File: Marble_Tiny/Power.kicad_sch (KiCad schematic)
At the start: 63 parts, among them J10 Barrel_Jack_Switch, Q4 DMP3013SFV, U10 TPSM863257RDXR, U11 TPSM863257RDXR, U18 TLV77325PDBVR, U20 RT9045AGSP / AP2303, U23 NCV59801CML120TCG, U24 SN74LVC1G07DBV, U25 SN74LVC1G07DBV, U4 TPSM863257RDXR, U5 TPSM863257RDXR, U6 TPSM863257RDXR

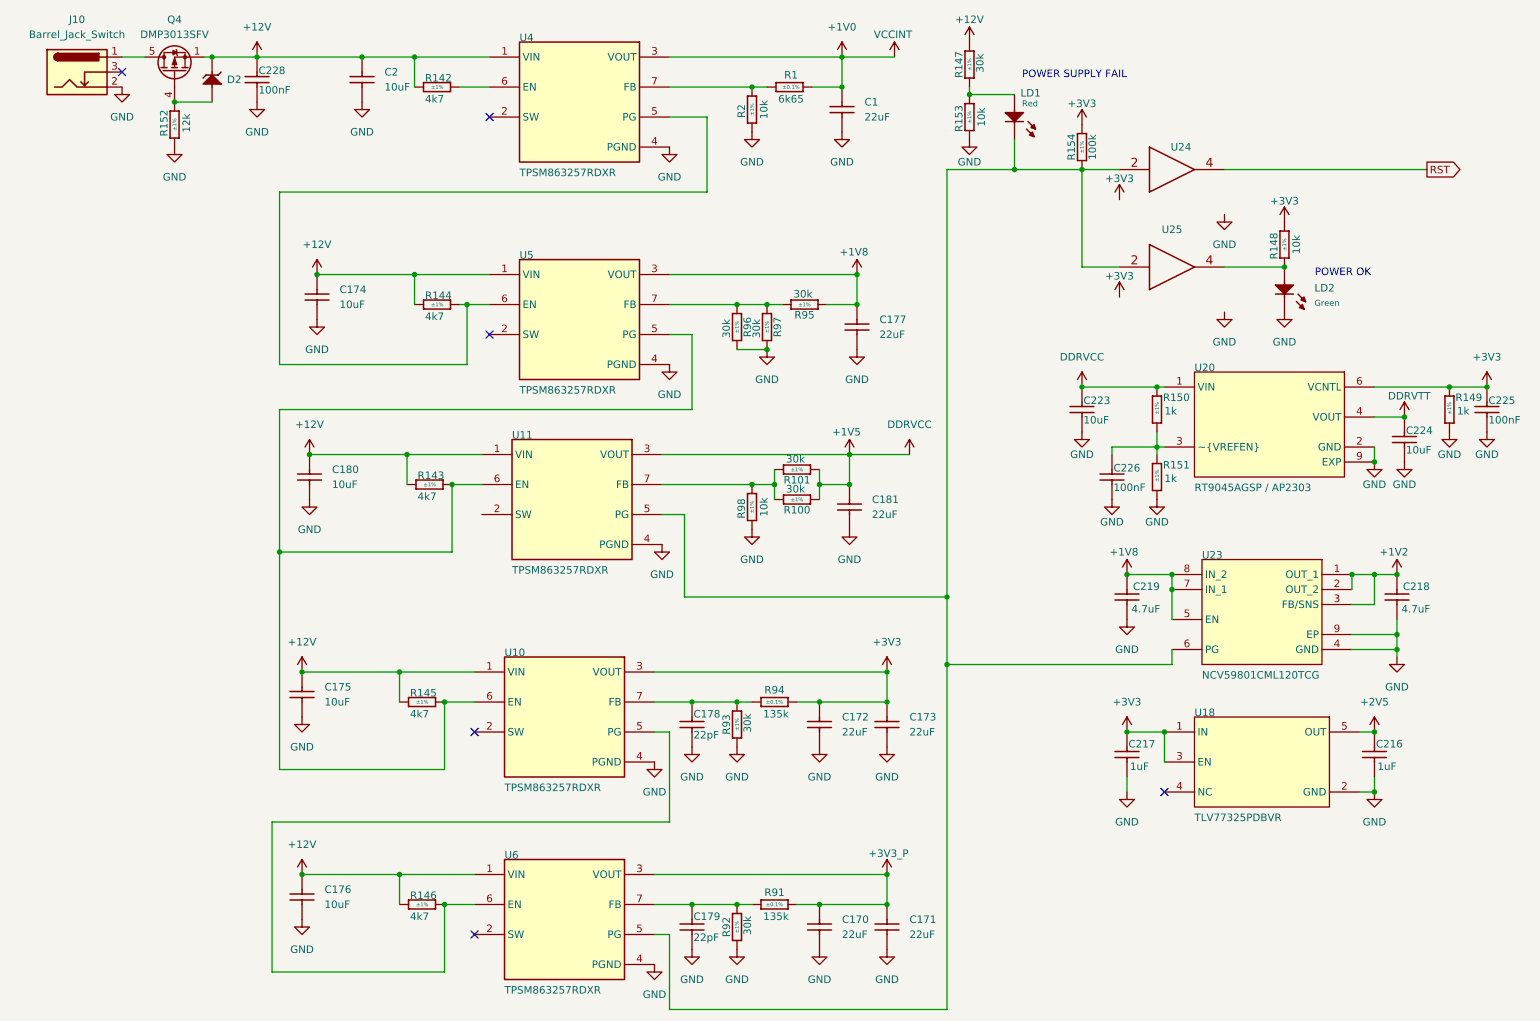
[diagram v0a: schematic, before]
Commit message: fixed ERCs; added test points; added WP switch
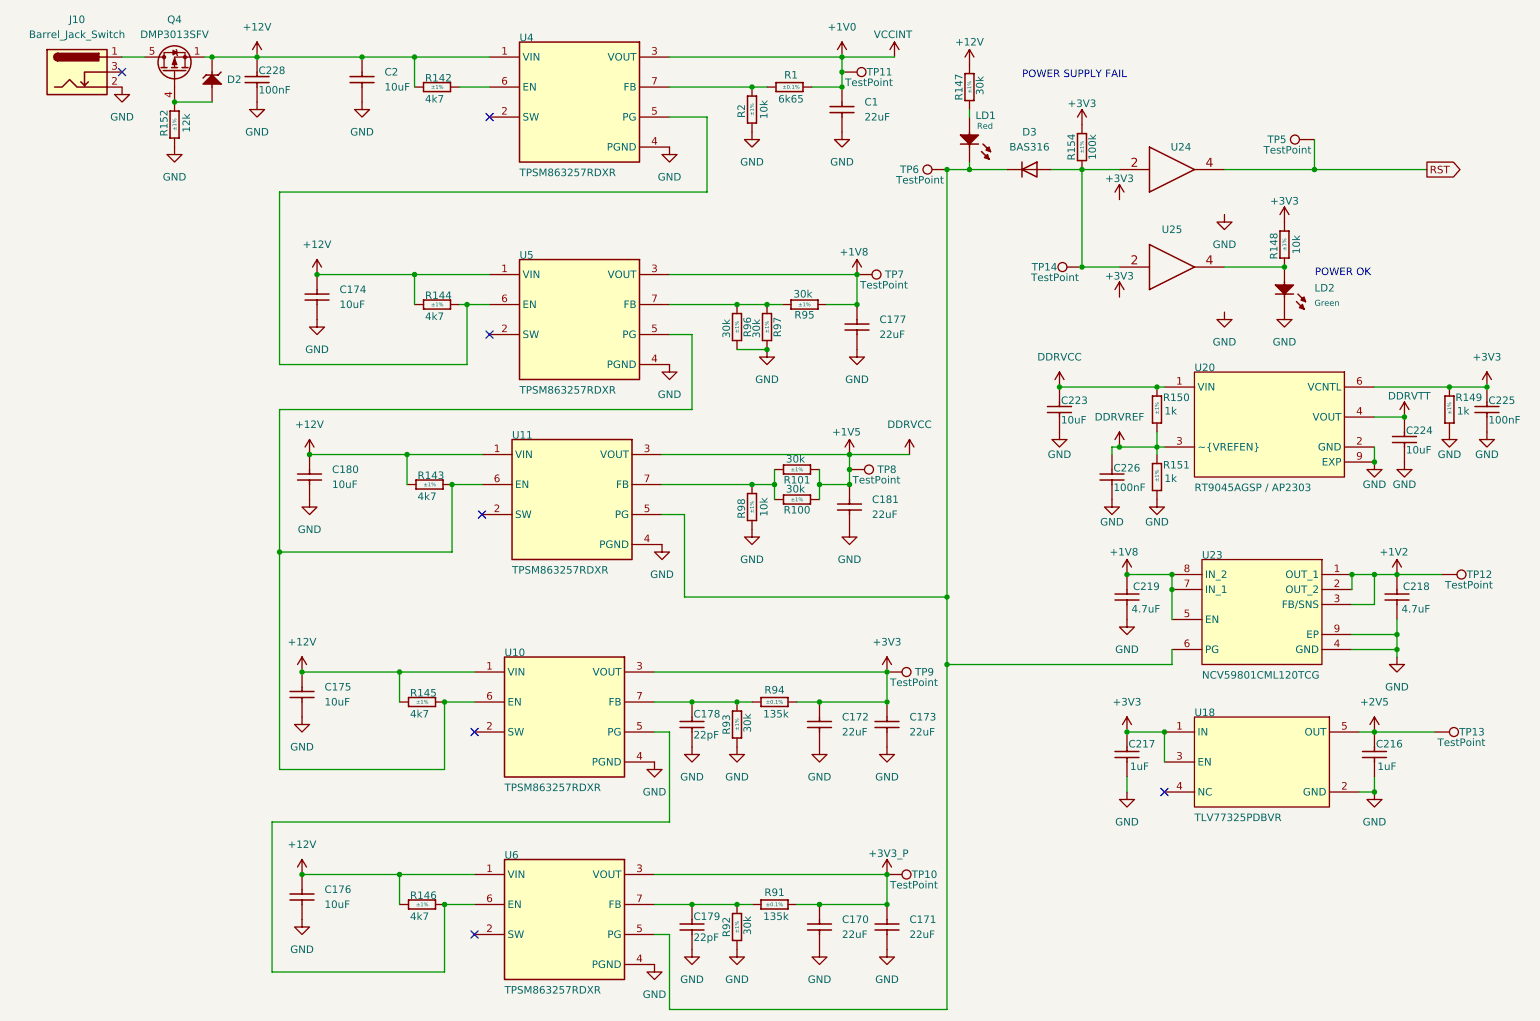
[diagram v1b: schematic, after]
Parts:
- removed R153: R0402_10K_1%_0.0625W_100PPM, Resistors SMD:RESC1005X40N, symbol Resistors SMD:R0402_10K_1%_0.0625W_100PPM
- added D3: BAS316, Diode_SMD:D_SOD-323, symbol Diode:BAS316
- added TP10, TP11, TP12, TP13, TP14, TP5, TP6, TP7, TP8, TP9: TestPoint, TestPoint:TestPoint_Pad_D1.5mm, symbol Connector:TestPoint
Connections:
- net +1V0: now also TP11.1
- net +1V2: now also TP12.1
- net +1V5: now also TP8.1
- net +1V8: now also TP7.1
- net +2V5: now also TP13.1
- net +3V3: now also TP9.1
- net +3V3_P: now also TP10.1
- net RST: now also TP5.1
- net DDRVREF: now reaches C226.2, R150.1, R151.2, U20.3 (~{VREFEN~{}})
- net at LD1.1 (C), U11.5 (PG), U23.6 (PG)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: now also D3.1 (K), TP6.1; no longer R154.2, U24.2 (IN), U25.2 (IN)
- new net: D3.2 (A), R154.2, TP14.1, U24.2 (IN), U25.2 (IN)
- no-connect marks 6 -> 7
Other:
- moved on the sheet: C223, LD1, R147

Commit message: fixed issue with PMODs; added board name and revision; fixed polygons issue
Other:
- company: (none) -> ${name}
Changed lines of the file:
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@@
 	(generator_version "9.0")
 	(paper "A4")
+	(title_block
+		(date "2025-04-18")
+		(rev "${rev}")
+		(company "${name}")
+		(comment 1 "${author}")
+	)
 	(text "POWER SUPPLY FAIL"
 		(exclude_from_sim no)
